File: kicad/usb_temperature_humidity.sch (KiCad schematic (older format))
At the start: 18 parts, among them J1 Conn_01x01, J10 Conn_01x01, J11 Conn_01x01, J12 Conn_01x01, J13 Conn_01x01, J14 Conn_01x01, J2 Conn_01x01, J3 Conn_01x01, J4 Conn_01x01, J5 Conn_01x01, J6 Conn_01x01, J7 Conn_01x01, J8 Conn_01x01, J9 Conn_01x01, U1 SeeeduinoXIAO, U2 SHT-31

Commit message: 使うか分からんけどスイッチ追加した
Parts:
- added R3, R4: R, Resistor_THT:R_Axial_DIN0207_L6.3mm_D2.5mm_P10.16mm_Horizontal, symbol Device:R
- added SW1, SW2: SW_SPDT, Mylib:SW_SLIDE_sengoku, symbol Switch:SW_SPDT
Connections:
- wire segments 36 -> 46
- no-connect marks 10 -> 12
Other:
- moved on the sheet: J1, J10, J11, J12, J13, J14, J2, J3, J4, J5, J6, J7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

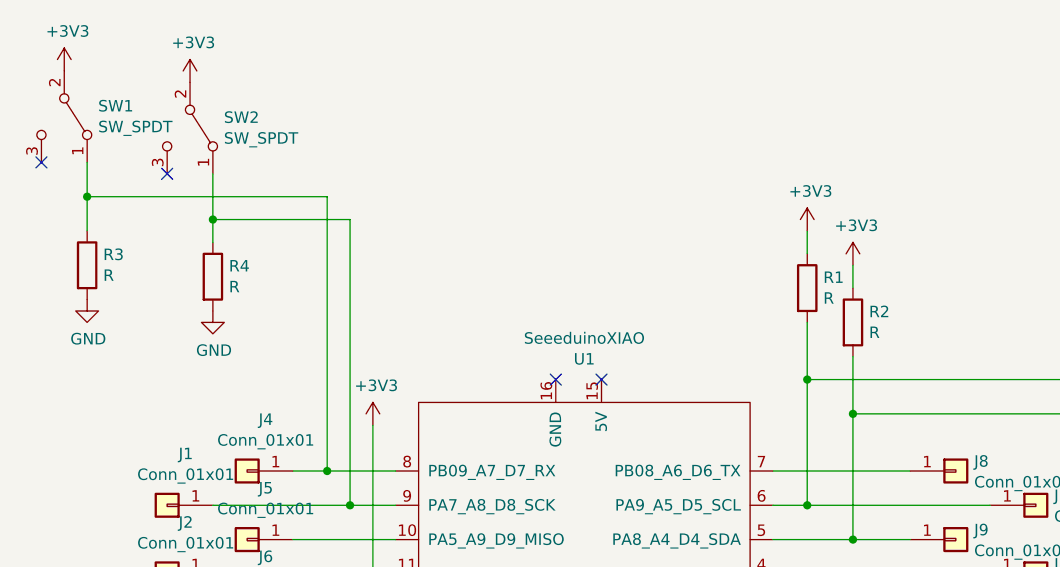
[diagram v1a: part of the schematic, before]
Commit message: 抵抗のナンバリングが気持ち悪かったので直した
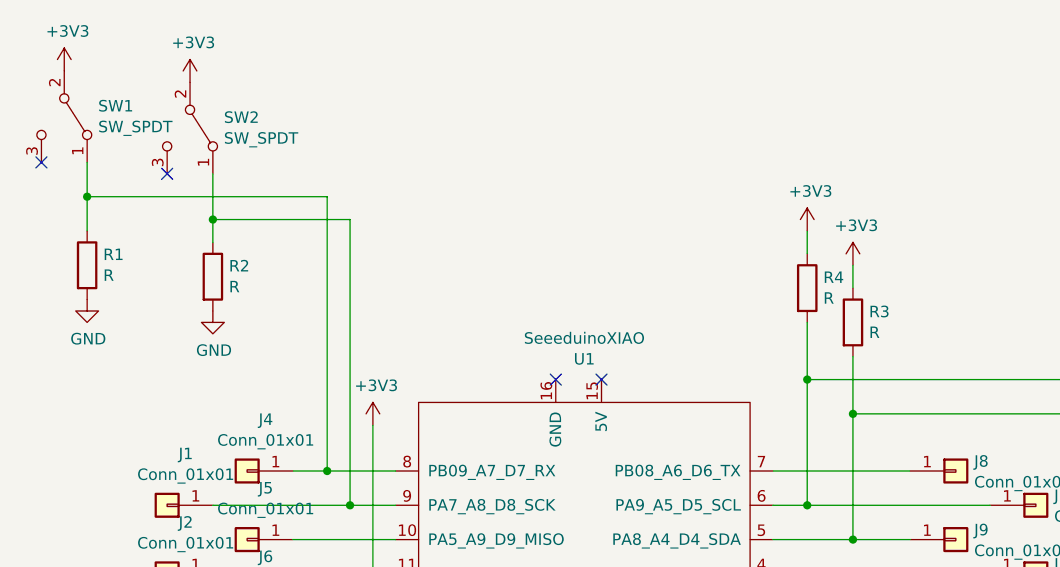
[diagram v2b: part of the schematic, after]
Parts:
- renumbered R3 to R1, R4 to R2, R2 to R3, R1 to R4
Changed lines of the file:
@@
 	4100 4500 4700 4500
 $Comp
-L Device:R R1
+L Device:R R4
 U 1 1 5F3FC51D
 P 4250 2800
-F 0 "R1" H 4320 2846 50  0000 L CNN
+F 0 "R4" H 4320 2846 50  0000 L CNN
 F 1 "R" H 4320 2755 50  0000 L CNN
 F 2 "Resistor_THT:R_Axial_DIN0207_L6.3mm_D2.5mm_P10.16mm_Horizontal" V 4180 2800 50  0001 C CNN
@@
 $EndComp
 $Comp
-L Device:R R2
+L Device:R R3
 U 1 1 5F3FC106
 P 4450 2950
-F 0 "R2" H 4520 2996 50  0000 L CNN
+F 0 "R3" H 4520 2996 50  0000 L CNN
 F 1 "R" H 4520 2905 50  0000 L CNN
 F 2 "Resistor_THT:R_Axial_DIN0207_L6.3mm_D2.5mm_P10.16mm_Horizontal" V 4380 2950 50  0001 C CNN
@@
 $EndComp
 $Comp
-L Device:R R3
+L Device:R R1
 U 1 1 5F452954
 P 1100 2700
-F 0 "R3" H 1170 2746 50  0000 L CNN
+F 0 "R1" H 1170 2746 50  0000 L CNN
 F 1 "R" H 1170 2655 50  0000 L CNN
 F 2 "Resistor_THT:R_Axial_DIN0207_L6.3mm_D2.5mm_P10.16mm_Horizontal" V 1030 2700 50  0001 C CNN
@@
 $EndComp
 $Comp
-L Device:R R4
+L Device:R R2
 U 1 1 5F45326C
 P 1650 2750
-F 0 "R4" H 1720 2796 50  0000 L CNN
+F 0 "R2" H 1720 2796 50  0000 L CNN
 F 1 "R" H 1720 2705 50  0000 L CNN
 F 2 "Resistor_THT:R_Axial_DIN0207_L6.3mm_D2.5mm_P10.16mm_Horizontal" V 1580 2750 50  0001 C CNN

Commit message: ピンヘッダのナンバリングが気持ち悪かったのでXIAOのピン番号に合わせた
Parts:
- renumbered J11 to J1, J5 to J10, J2 to J11, J6 to J12, J3 to J13, J7 to J14, J14 to J2, J10 to J3, J13 to J4, J9 to J5, J12 to J6, J8 to J7, J4 to J8, J1 to J9
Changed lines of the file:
@@
 $EndComp
 $Comp
-L Connector_Generic:Conn_01x01 J11
+L Connector_Generic:Conn_01x01 J1
 U 1 1 5F405C41
 P 4900 4500
-F 0 "J11" H 4980 4542 50  0000 L CNN
+F 0 "J1" H 4980 4542 50  0000 L CNN
 F 1 "Conn_01x01" H 4980 4451 50  0000 L CNN
 F 2 "Connector_PinHeader_2.54mm:PinHeader_1x01_P2.54mm_Vertical" H 4900 4500 50  0001 C CNN
@@
 $EndComp
 $Comp
-L Connector_Generic:Conn_01x01 J14
+L Connector_Generic:Conn_01x01 J2
 U 1 1 5F406D89
 P 5250 4350
-F 0 "J14" H 5330 4392 50  0000 L CNN
+F 0 "J2" H 5330 4392 50  0000 L CNN
 F 1 "Conn_01x01" H 5330 4301 50  0000 L CNN
 F 2 "Connector_PinHeader_2.54mm:PinHeader_1x01_P2.54mm_Vertical" H 5250 4350 50  0001 C CNN
@@
 $EndComp
 $Comp
-L Connector_Generic:Conn_01x01 J10
+L Connector_Generic:Conn_01x01 J3
 U 1 1 5F40748E
 P 4900 4200
-F 0 "J10" H 4980 4242 50  0000 L CNN
+F 0 "J3" H 4980 4242 50  0000 L CNN
 F 1 "Conn_01x01" H 4980 4151 50  0000 L CNN
 F 2 "Connector_PinHeader_2.54mm:PinHeader_1x01_P2.54mm_Vertical" H 4900 4200 50  0001 C CNN
@@
 $EndComp
 $Comp
-L Connector_Generic:Conn_01x01 J13
+L Connector_Generic:Conn_01x01 J4
 U 1 1 5F407774
 P 5250 4050
-F 0 "J13" H 5330 4092 50  0000 L CNN
+F 0 "J4" H 5330 4092 50  0000 L CNN
 F 1 "Conn_01x01" H 5330 4001 50  0000 L CNN
 F 2 "Connector_PinHeader_2.54mm:PinHeader_1x01_P2.54mm_Vertical" H 5250 4050 50  0001 C CNN
@@
 $EndComp
 $Comp
-L Connector_Generic:Conn_01x01 J9
+L Connector_Generic:Conn_01x01 J5
 U 1 1 5F407983
 P 4900 3900
-F 0 "J9" H 4980 3942 50  0000 L CNN
+F 0 "J5" H 4980 3942 50  0000 L CNN
 F 1 "Conn_01x01" H 4980 3851 50  0000 L CNN
 F 2 "Connector_PinHeader_2.54mm:PinHeader_1x01_P2.54mm_Vertical" H 4900 3900 50  0001 C CNN
@@
 $EndComp
 $Comp
-L Connector_Generic:Conn_01x01 J12
+L Connector_Generic:Conn_01x01 J6
 U 1 1 5F407CF2
 P 5250 3750
-F 0 "J12" H 5330 3792 50  0000 L CNN
+F 0 "J6" H 5330 3792 50  0000 L CNN
 F 1 "Conn_01x01" H 5330 3701 50  0000 L CNN
 F 2 "Connector_PinHeader_2.54mm:PinHeader_1x01_P2.54mm_Vertical" H 5250 3750 50  0001 C CNN
@@
 $EndComp
 $Comp
-L Connector_Generic:Conn_01x01 J8
+L Connector_Generic:Conn_01x01 J7
 U 1 1 5F40823F
 P 4900 3600
-F 0 "J8" H 4980 3642 50  0000 L CNN
+F 0 "J7" H 4980 3642 50  0000 L CNN
 F 1 "Conn_01x01" H 4980 3551 50  0000 L CNN
 F 2 "Connector_PinHeader_2.54mm:PinHeader_1x01_P2.54mm_Vertical" H 4900 3600 50  0001 C CNN
@@
 $EndComp
 $Comp
-L Connector_Generic:Conn_01x01 J7
+L Connector_Generic:Conn_01x01 J14
 U 1 1 5F4088EC
 P 1800 4500
-F 0 "J7" H 1718 4275 50  0000 C CNN
+F 0 "J14" H 1718 4275 50  0000 C CNN
 F 1 "Conn_01x01" H 1718 4366 50  0000 C CNN
 F 2 "Connector_PinHeader_2.54mm:PinHeader_1x01_P2.54mm_Vertical" H 1800 4500 50  0001 C CNN
@@
 $EndComp
 $Comp
-L Connector_Generic:Conn_01x01 J3
+L Connector_Generic:Conn_01x01 J13
 U 1 1 5F40977D
 P 1450 4350
-F 0 "J3" H 1368 4125 50  0000 C CNN
+F 0 "J13" H 1368 4125 50  0000 C CNN
 F 1 "Conn_01x01" H 1368 4216 50  0000 C CNN
 F 2 "Connector_PinHeader_2.54mm:PinHeader_1x01_P2.54mm_Vertical" H 1450 4350 50  0001 C CNN
@@
 $EndComp
 $Comp
-L Connector_Generic:Conn_01x01 J6
+L Connector_Generic:Conn_01x01 J12
 U 1 1 5F40AB06
 P 1800 4200
-F 0 "J6" H 1718 3975 50  0000 C CNN
+F 0 "J12" H 1718 3975 50  0000 C CNN
 F 1 "Conn_01x01" H 1718 4066 50  0000 C CNN
 F 2 "Connector_PinHeader_2.54mm:PinHeader_1x01_P2.54mm_Vertical" H 1800 4200 50  0001 C CNN
@@
 $EndComp
 $Comp
-L Connector_Generic:Conn_01x01 J2
+L Connector_Generic:Conn_01x01 J11
 U 1 1 5F40AB0C
 P 1450 4050
-F 0 "J2" H 1368 3825 50  0000 C CNN
+F 0 "J11" H 1368 3825 50  0000 C CNN
 F 1 "Conn_01x01" H 1368 3916 50  0000 C CNN
 F 2 "Connector_PinHeader_2.54mm:PinHeader_1x01_P2.54mm_Vertical" H 1450 4050 50  0001 C CNN
@@
 $EndComp
 $Comp
-L Connector_Generic:Conn_01x01 J5
+L Connector_Generic:Conn_01x01 J10
 U 1 1 5F40B750
 P 1800 3900
-F 0 "J5" H 1718 3675 50  0000 C CNN
+F 0 "J10" H 1718 3675 50  0000 C CNN
 F 1 "Conn_01x01" H 1718 3766 50  0000 C CNN
 F 2 "Connector_PinHeader_2.54mm:PinHeader_1x01_P2.54mm_Vertical" H 1800 3900 50  0001 C CNN
@@
 $EndComp
 $Comp
-L Connector_Generic:Conn_01x01 J1
+L Connector_Generic:Conn_01x01 J9
 U 1 1 5F40B756
 P 1450 3750
-F 0 "J1" H 1368 3525 50  0000 C CNN
+F 0 "J9" H 1368 3525 50  0000 C CNN
 F 1 "Conn_01x01" H 1368 3616 50  0000 C CNN
 F 2 "Connector_PinHeader_2.54mm:PinHeader_1x01_P2.54mm_Vertical" H 1450 3750 50  0001 C CNN
@@
 $EndComp
 $Comp
-L Connector_Generic:Conn_01x01 J4
+L Connector_Generic:Conn_01x01 J8
 U 1 1 5F40BF8E
 P 1800 3600
-F 0 "J4" H 1718 3375 50  0000 C CNN
+F 0 "J8" H 1718 3375 50  0000 C CNN
 F 1 "Conn_01x01" H 1718 3466 50  0000 C CNN
 F 2 "Connector_PinHeader_2.54mm:PinHeader_1x01_P2.54mm_Vertical" H 1800 3600 50  0001 C CNN

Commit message: フットプリントの更新と、SHT-31のADDRピンをGNDに落とした
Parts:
- removed U2: SHT-31, SHT-31:SHT-31, symbol SHT-31:SHT-31
- added U2: SHT-31, kicad_mylib:SHT-31, symbol kicad_mylib:SHT-31
- SW1, SW2: footprint Mylib:SW_SLIDE_sengoku -> kicad_mylib:SW_SLIDE_sengoku
- U1: footprint Seeeduino XIAO:Seeeduino XIAO-MOUDLE14P-2.54-21X17.8MM -> kicad_mylib:SeeedXIAO
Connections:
- wire segments 46 -> 50
- no-connect marks 12 -> 10
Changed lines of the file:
@@
 	900  1050 900  1200
-$Comp
-L SHT-31:SHT-31 U2
-U 1 1 5F3FADA2
-P 6150 3600
-F 0 "U2" H 6450 4415 50  0000 C CNN
-F 1 "SHT-31" H 6450 4324 50  0000 C CNN
-F 2 "SHT-31:SHT-31" H 6700 4300 50  0001 C CNN
-F 3 "" H 6700 4300 50  0001 C CNN
-	1    6150 3600
-	1    0    0    -1
-$EndComp
 $Comp
 L power:+3V3 #PWR03
@@
 F 0 "U1" H 3225 3111 50  0000 C CNN
 F 1 "SeeeduinoXIAO" H 3225 3020 50  0000 C CNN
-F 2 "Seeeduino XIAO:Seeeduino XIAO-MOUDLE14P-2.54-21X17.8MM" H 2900 4250 50  0001 C CNN
+F 2 "kicad_mylib:SeeedXIAO" H 2900 4250 50  0001 C CNN
 F 3 "" H 2900 4250 50  0001 C CNN
 	1    3250 4050
@@
 NoConn ~ 6850 3050
 NoConn ~ 6850 3200
-NoConn ~ 6850 3350
-NoConn ~ 6850 3500
 NoConn ~ 3350 3200
 NoConn ~ 3150 3200
@@
 F 0 "SW1" V 954 2198 50  0000 L CNN
 F 1 "SW_SPDT" V 1045 2198 50  0000 L CNN
-F 2 "Mylib:SW_SLIDE_sengoku" H 1000 2050 50  0001 C CNN
+F 2 "kicad_mylib:SW_SLIDE_sengoku" H 1000 2050 50  0001 C CNN
 F 3 "~" H 1000 2050 50  0001 C CNN
 	1    1000 2050
@@
 F 0 "SW2" V 1504 2248 50  0000 L CNN
 F 1 "SW_SPDT" V 1595 2248 50  0000 L CNN
-F 2 "Mylib:SW_SLIDE_sengoku" H 1550 2100 50  0001 C CNN
+F 2 "kicad_mylib:SW_SLIDE_sengoku" H 1550 2100 50  0001 C CNN
 F 3 "~" H 1550 2100 50  0001 C CNN
 	1    1550 2100
@@
 NoConn ~ 1450 2300
 NoConn ~ 900  2250
+$Comp
+L kicad_mylib:SHT-31 U2
+U 1 1 5FB3D220
+P 6150 3600
+F 0 "U2" H 6450 4415 50  0000 C CNN
+F 1 "SHT-31" H 6450 4324 50  0000 C CNN
+F 2 "kicad_mylib:SHT-31" H 6700 4300 50  0001 C CNN
+F 3 "" H 6700 4300 50  0001 C CNN
+	1    6150 3600
+	1    0    0    -1
+$EndComp
+$Comp
+L power:GND #PWR013
+U 1 1 5FB42E84
+P 6950 3700
+F 0 "#PWR013" H 6950 3450 50  0001 C CNN
+F 1 "GND" H 6955 3527 50  0000 C CNN
+F 2 "" H 6950 3700 50  0001 C CNN
+F 3 "" H 6950 3700 50  0001 C CNN
+	1    6950 3700
+	1    0    0    -1
+$EndComp
+Wire Wire Line
+	6850 3350 6950 3350
+Wire Wire Line
+	6950 3350 6950 3500
+Wire Wire Line
+	6850 3500 6950 3500
+Connection ~ 6950 3500
+Wire Wire Line
+	6950 3500 6950 3700
 $EndSCHEMATC

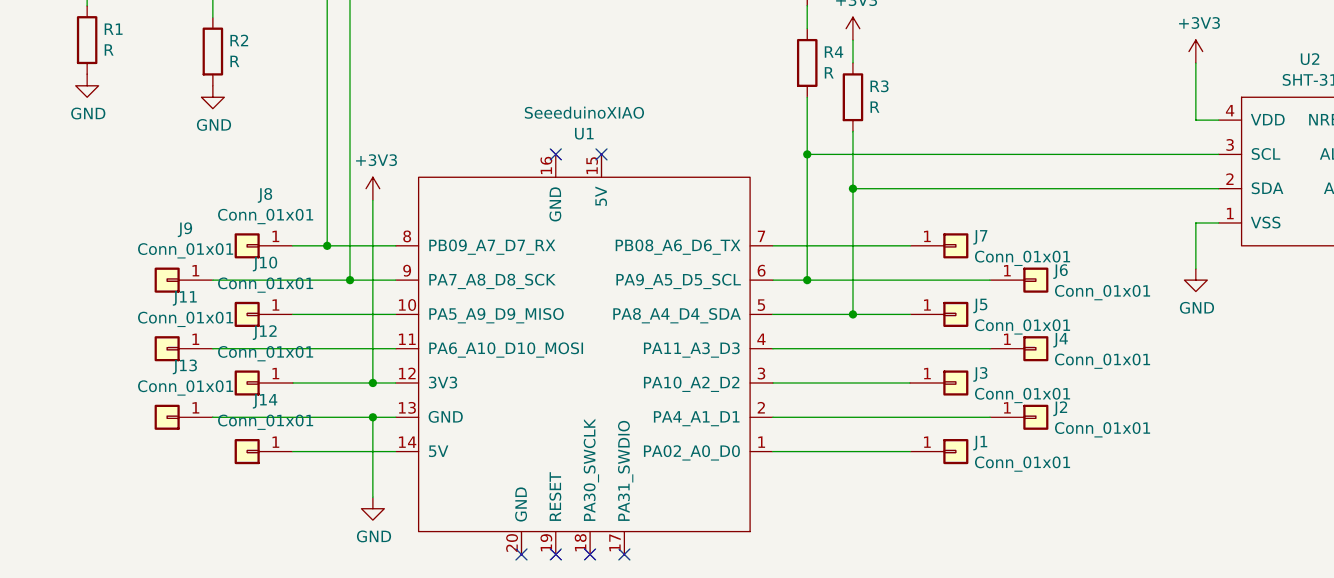
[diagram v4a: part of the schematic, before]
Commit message: XIAOのピンヘッダを1x1の標準ライブラリから1x7の自作ライブラリに変えた
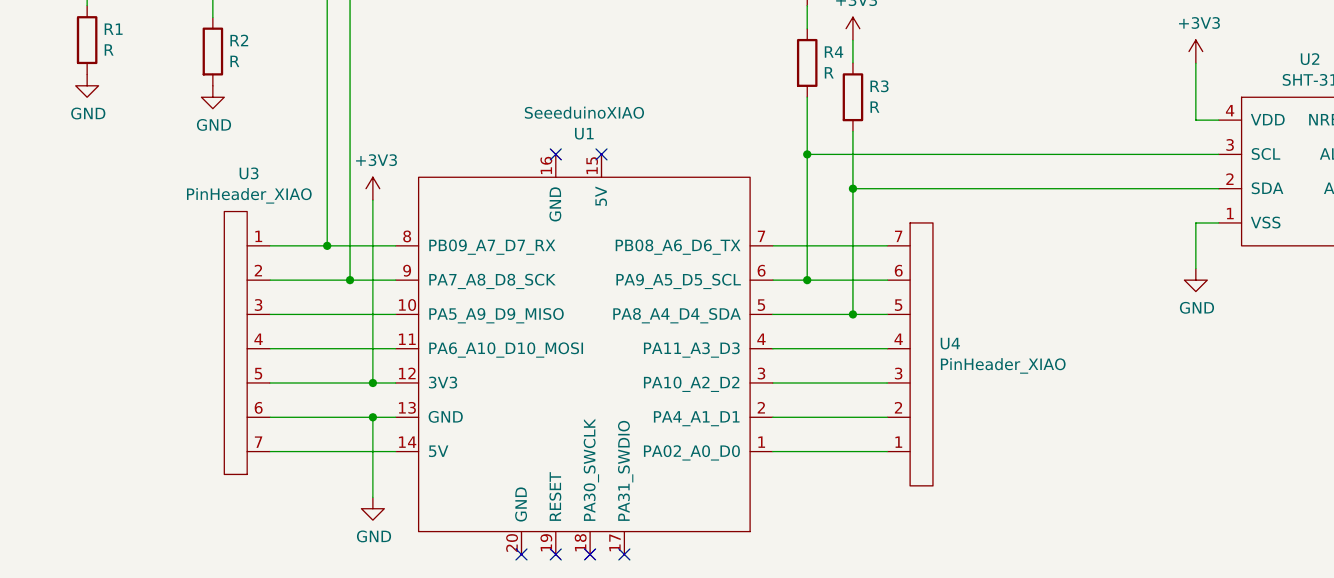
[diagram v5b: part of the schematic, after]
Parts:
- removed J1, J10, J11, J12, J13, J14, J2, J3, J4, J5, J6, J7, J8, J9: Conn_01x01, Connector_PinHeader_2.54mm:PinHeader_1x01_P2.54mm_Vertical, symbol Connector_Generic:Conn_01x01
- added U3, U4: PinHeader_XIAO, kicad_mylib:PinHeader_XIAO, symbol kicad_mylib:PinHeader_XIAO
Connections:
- net +3V3: now also U3.5
- net GND: now also U3.6
- net at U1.1 (PA02_A0_D0): now also U4.1
- net at U1.10 (PA5_A9_D9_MISO): now also U3.3
- net at U1.11 (PA6_A10_D10_MOSI): now also U3.4
- net at U1.14 (5V): now also U3.7
- net at U1.2 (PA4_A1_D1): now also U4.2
- net at U1.3 (PA10_A2_D2): now also U4.3
- net at U1.4 (PA11_A3_D3): now also U4.4
- net at R3.2, U1.5 (PA8_A4_D4_SDA), U2.2 (SDA): now also U4.5
- net at R4.2, U1.6 (PA9_A5_D5_SCL), U2.3 (SCL): now also U4.6
- net at U1.7 (PB08_A6_D6_TX): now also U4.7
- net at R1.1, SW1.1 (A), U1.8 (PB09_A7_D7_RX): now also U3.1
- net at R2.1, SW2.1 (A), U1.9 (PA7_A8_D8_SCK): now also U3.2
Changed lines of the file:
@@
-$EndComp
-$Comp
-L Connector_Generic:Conn_01x01 J1
-U 1 1 5F405C41
-P 4900 4500
-F 0 "J1" H 4980 4542 50  0000 L CNN
-F 1 "Conn_01x01" H 4980 4451 50  0000 L CNN
-F 2 "Connector_PinHeader_2.54mm:PinHeader_1x01_P2.54mm_Vertical" H 4900 4500 50  0001 C CNN
-F 3 "~" H 4900 4500 50  0001 C CNN
-	1    4900 4500
-	1    0    0    -1
-$EndComp
-$Comp
-L Connector_Generic:Conn_01x01 J2
-U 1 1 5F406D89
-P 5250 4350
-F 0 "J2" H 5330 4392 50  0000 L CNN
-F 1 "Conn_01x01" H 5330 4301 50  0000 L CNN
-F 2 "Connector_PinHeader_2.54mm:PinHeader_1x01_P2.54mm_Vertical" H 5250 4350 50  0001 C CNN
-F 3 "~" H 5250 4350 50  0001 C CNN
-	1    5250 4350
-	1    0    0    -1
-$EndComp
-$Comp
-L Connector_Generic:Conn_01x01 J3
-U 1 1 5F40748E
-P 4900 4200
-F 0 "J3" H 4980 4242 50  0000 L CNN
-F 1 "Conn_01x01" H 4980 4151 50  0000 L CNN
-F 2 "Connector_PinHeader_2.54mm:PinHeader_1x01_P2.54mm_Vertical" H 4900 4200 50  0001 C CNN
-F 3 "~" H 4900 4200 50  0001 C CNN
-	1    4900 4200
-	1    0    0    -1
-$EndComp
-$Comp
-L Connector_Generic:Conn_01x01 J4
-U 1 1 5F407774
-P 5250 4050
-F 0 "J4" H 5330 4092 50  0000 L CNN
-F 1 "Conn_01x01" H 5330 4001 50  0000 L CNN
-F 2 "Connector_PinHeader_2.54mm:PinHeader_1x01_P2.54mm_Vertical" H 5250 4050 50  0001 C CNN
-F 3 "~" H 5250 4050 50  0001 C CNN
-	1    5250 4050
-	1    0    0    -1
-$EndComp
-$Comp
-L Connector_Generic:Conn_01x01 J5
-U 1 1 5F407983
-P 4900 3900
-F 0 "J5" H 4980 3942 50  0000 L CNN
-F 1 "Conn_01x01" H 4980 3851 50  0000 L CNN
-F 2 "Connector_PinHeader_2.54mm:PinHeader_1x01_P2.54mm_Vertical" H 4900 3900 50  0001 C CNN
-F 3 "~" H 4900 3900 50  0001 C CNN
-	1    4900 3900
-	1    0    0    -1
-$EndComp
-$Comp
-L Connector_Generic:Conn_01x01 J6
-U 1 1 5F407CF2
-P 5250 3750
-F 0 "J6" H 5330 3792 50  0000 L CNN
-F 1 "Conn_01x01" H 5330 3701 50  0000 L CNN
-F 2 "Connector_PinHeader_2.54mm:PinHeader_1x01_P2.54mm_Vertical" H 5250 3750 50  0001 C CNN
-F 3 "~" H 5250 3750 50  0001 C CNN
-	1    5250 3750
-	1    0    0    -1
-$EndComp
-$Comp
-L Connector_Generic:Conn_01x01 J7
-U 1 1 5F40823F
-P 4900 3600
-F 0 "J7" H 4980 3642 50  0000 L CNN
-F 1 "Conn_01x01" H 4980 3551 50  0000 L CNN
-F 2 "Connector_PinHeader_2.54mm:PinHeader_1x01_P2.54mm_Vertical" H 4900 3600 50  0001 C CNN
-F 3 "~" H 4900 3600 50  0001 C CNN
-	1    4900 3600
-	1    0    0    -1
-$EndComp
-$Comp
-L Connector_Generic:Conn_01x01 J14
-U 1 1 5F4088EC
-P 1800 4500
-F 0 "J14" H 1718 4275 50  0000 C CNN
-F 1 "Conn_01x01" H 1718 4366 50  0000 C CNN
-F 2 "Connector_PinHeader_2.54mm:PinHeader_1x01_P2.54mm_Vertical" H 1800 4500 50  0001 C CNN
-F 3 "~" H 1800 4500 50  0001 C CNN
-	1    1800 4500
-	-1   0    0    1
-$EndComp
-$Comp
-L Connector_Generic:Conn_01x01 J13
-U 1 1 5F40977D
-P 1450 4350
-F 0 "J13" H 1368 4125 50  0000 C CNN
-F 1 "Conn_01x01" H 1368 4216 50  0000 C CNN
-F 2 "Connector_PinHeader_2.54mm:PinHeader_1x01_P2.54mm_Vertical" H 1450 4350 50  0001 C CNN
-F 3 "~" H 1450 4350 50  0001 C CNN
-	1    1450 4350
-	-1   0    0    1
-$EndComp
-$Comp
-L Connector_Generic:Conn_01x01 J12
-U 1 1 5F40AB06
-P 1800 4200
-F 0 "J12" H 1718 3975 50  0000 C CNN
-F 1 "Conn_01x01" H 1718 4066 50  0000 C CNN
-F 2 "Connector_PinHeader_2.54mm:PinHeader_1x01_P2.54mm_Vertical" H 1800 4200 50  0001 C CNN
-F 3 "~" H 1800 4200 50  0001 C CNN
-	1    1800 4200
-	-1   0    0    1
-$EndComp
-$Comp
-L Connector_Generic:Conn_01x01 J11
-U 1 1 5F40AB0C
-P 1450 4050
-F 0 "J11" H 1368 3825 50  0000 C CNN
-F 1 "Conn_01x01" H 1368 3916 50  0000 C CNN
-F 2 "Connector_PinHeader_2.54mm:PinHeader_1x01_P2.54mm_Vertical" H 1450 4050 50  0001 C CNN
-F 3 "~" H 1450 4050 50  0001 C CNN
-	1    1450 4050
-	-1   0    0    1
-$EndComp
-$Comp
-L Connector_Generic:Conn_01x01 J10
-U 1 1 5F40B750
-P 1800 3900
-F 0 "J10" H 1718 3675 50  0000 C CNN
-F 1 "Conn_01x01" H 1718 3766 50  0000 C CNN
-F 2 "Connector_PinHeader_2.54mm:PinHeader_1x01_P2.54mm_Vertical" H 1800 3900 50  0001 C CNN
-F 3 "~" H 1800 3900 50  0001 C CNN
-	1    1800 3900
-	-1   0    0    1
-$EndComp
-$Comp
-L Connector_Generic:Conn_01x01 J9
-U 1 1 5F40B756
-P 1450 3750
-F 0 "J9" H 1368 3525 50  0000 C CNN
-F 1 "Conn_01x01" H 1368 3616 50  0000 C CNN
-F 2 "Connector_PinHeader_2.54mm:PinHeader_1x01_P2.54mm_Vertical" H 1450 3750 50  0001 C CNN
-F 3 "~" H 1450 3750 50  0001 C CNN
-	1    1450 3750
-	-1   0    0    1
-$EndComp
-$Comp
-L Connector_Generic:Conn_01x01 J8
-U 1 1 5F40BF8E
-P 1800 3600
-F 0 "J8" H 1718 3375 50  0000 C CNN
-F 1 "Conn_01x01" H 1718 3466 50  0000 C CNN
-F 2 "Connector_PinHeader_2.54mm:PinHeader_1x01_P2.54mm_Vertical" H 1800 3600 50  0001 C CNN
-F 3 "~" H 1800 3600 50  0001 C CNN
-	1    1800 3600
-	-1   0    0    1
 $EndComp
 $Comp
@@
 	2450 3750 2250 3750
 Wire Wire Line
-	2000 3900 2450 3900
-Wire Wire Line
-	2450 4050 1650 4050
-Wire Wire Line
 	2450 4350 2350 4350
 Wire Wire Line
-	2000 4500 2450 4500
-Wire Wire Line
 	2350 4350 2350 4700
 Wire Wire Line
 	2350 3400 2350 4200
 Wire Wire Line
-	4100 3600 4700 3600
-Wire Wire Line
-	5050 3750 4250 3750
-Connection ~ 4250 3750
-Wire Wire Line
 	4250 3750 4100 3750
 Wire Wire Line
 	4100 3900 4450 3900
-Connection ~ 4450 3900
-Wire Wire Line
-	4450 3900 4700 3900
-Wire Wire Line
-	5050 4050 4100 4050
-Wire Wire Line
-	4100 4200 4700 4200
-Wire Wire Line
-	5050 4350 4100 4350
-Wire Wire Line
-	4100 4500 4700 4500
 $Comp
 L Device:R R4
@@
 	1    0    0    -1
 $EndComp
-Connection ~ 2350 4350
-Wire Wire Line
-	1650 4350 2350 4350
-Connection ~ 2350 4200
 Wire Wire Line
 	2350 4200 2450 4200
-Wire Wire Line
-	2000 4200 2350 4200
 Wire Wire Line
 	1650 2500 2250 2500
@@
 Wire Wire Line
 	1650 2500 1650 2600
-Connection ~ 2250 3750
-Wire Wire Line
-	2250 3750 1650 3750
 $Comp
 L Switch:SW_SPDT SW2
@@
 	1100 2250 1100 2400
 Wire Wire Line
-	2000 3600 2150 3600
-Wire Wire Line
 	1100 2400 2150 2400
 Wire Wire Line
@@
 Wire Wire Line
 	1100 2400 1100 2550
-Connection ~ 2150 3600
 Wire Wire Line
 	2150 3600 2450 3600
@@
 Wire Wire Line
 	6950 3500 6950 3700
+$Comp
+L kicad_mylib:PinHeader_XIAO U4
+U 1 1 5FB5C045
+P 4700 4650
+F 0 "U4" H 4828 5271 50  0000 L CNN
+F 1 "PinHeader_XIAO" H 4828 5180 50  0000 L CNN
+F 2 "kicad_mylib:PinHeader_XIAO" H 4750 5900 50  0001 C CNN
+F 3 "" H 4750 5900 50  0001 C CNN
+	1    4700 4650
+	1    0    0    -1
+$EndComp
+$Comp
+L kicad_mylib:PinHeader_XIAO U3
+U 1 1 5FB5D5B3
+P 1800 3450
+F 0 "U3" H 1792 3285 50  0000 C CNN
+F 1 "PinHeader_XIAO" H 1792 3376 50  0000 C CNN
+F 2 "kicad_mylib:PinHeader_XIAO" H 1850 4700 50  0001 C CNN
+F 3 "" H 1850 4700 50  0001 C CNN
+	1    1800 3450
+	-1   0    0    1
+$EndComp
+Wire Wire Line
+	4600 4500 4100 4500
+Wire Wire Line
+	4600 4350 4100 4350
+Wire Wire Line
+	4600 4200 4100 4200
+Wire Wire Line
+	4100 4050 4600 4050
+Wire Wire Line
+	4600 3900 4450 3900
+Connection ~ 4450 3900
+Wire Wire Line
+	4600 3750 4250 3750
+Connection ~ 4250 3750
+Wire Wire Line
+	4100 3600 4600 3600
+Wire Wire Line
+	2150 3600 1900 3600
+Connection ~ 2150 3600
+Wire Wire Line
+	1900 3750 2250 3750
+Connection ~ 2250 3750
+Wire Wire Line
+	1900 3900 2450 3900
+Wire Wire Line
+	1900 4050 2450 4050
+Wire Wire Line
+	2350 4200 1900 4200
+Connection ~ 2350 4200
+Wire Wire Line
+	1900 4350 2350 4350
+Connection ~ 2350 4350
+Wire Wire Line
+	1900 4500 2450 4500
 $EndSCHEMATC
